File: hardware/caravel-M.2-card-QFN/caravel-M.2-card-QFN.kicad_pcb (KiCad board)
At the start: 4 copper layers, 22 x 22 mm, 13 parts, among them J1 MICROMOD-2222-Generic, T1 Logo, T2 Logo, U1 Caravel

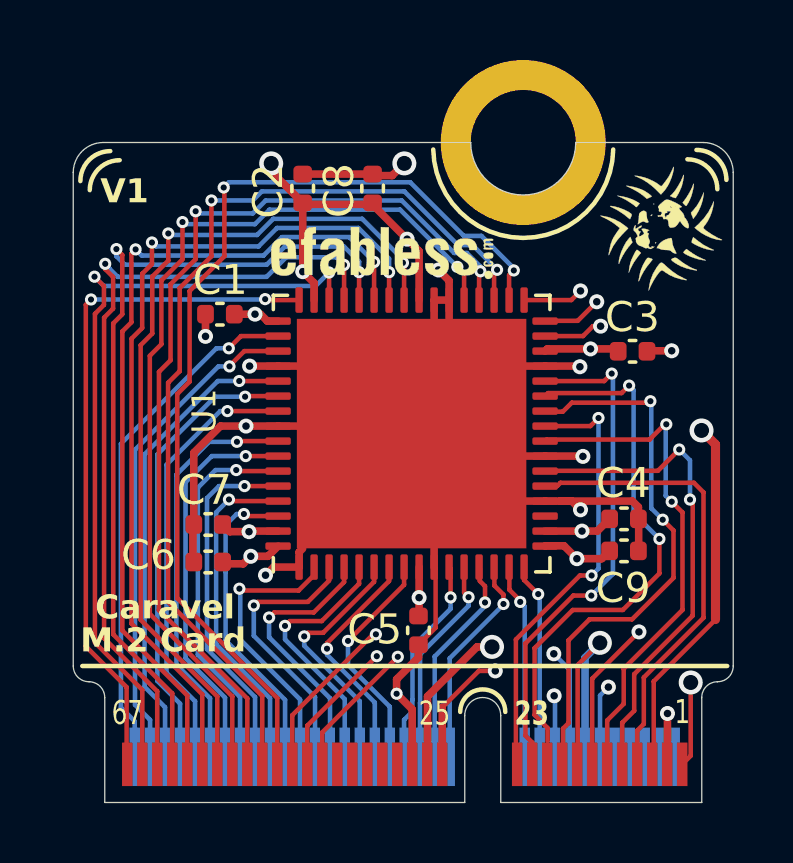
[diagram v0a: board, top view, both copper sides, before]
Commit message: update Caravel M.2 card PCBs - remove copper fill at the card edge to avoid shorts when the card is inserted in the M.2 connector
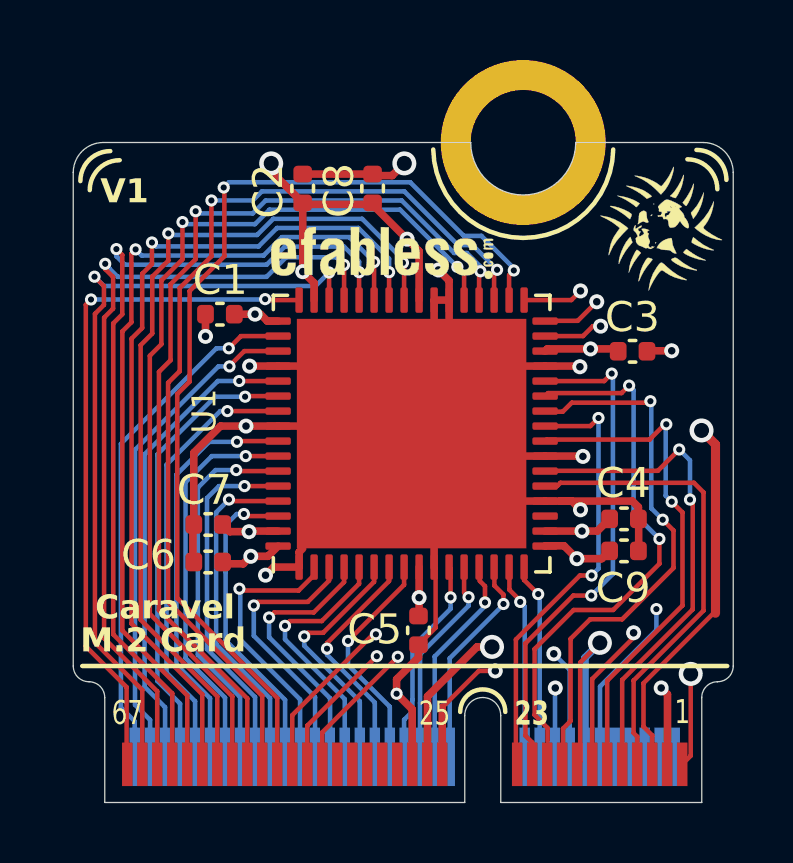
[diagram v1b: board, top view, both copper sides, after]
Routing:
- net GND: track 73.4 -> 76.9 mm
- net vddio: track 20.6 -> 21.6 mm
